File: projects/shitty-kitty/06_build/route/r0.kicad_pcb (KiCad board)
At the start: 4 copper layers, 130 x 75 mm, 82 parts, among them J1 DC-005C-20A 12V, J2 TYPE-C-31-M-12, J3 ELECTRODES INNER, J4 ELECTRODES OUTER, J5 MOTOR NEMA17, J6 ENDSTOP TERM, J8 HOST 1x6, Q1 AOD4185 revpol, SW1 TS-1187A BOOT, SW2 TS-1187A RESET, U1 ESP32-S3-WROOM-1-N8R2, U2 TMC2209-LA-T, U3 MPR121QR2 0x5A, U4 MPR121QR2 0x5B, U5 MPR121QR2 0x5C, U6 MPR121QR2 0x5D, U7 LIS2DH12TR, U8 AP63205WU-7, U9 AMS1117-3.3

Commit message: shitty-kitty: fab-floor pin for KRT (no advanced-via escalation), honest hole floors (h2h 0.3/holeclr 0.2), ELEC/3V3 width floors match router grading, route_surgery tool, stitcher fine-pitch GND rescue + via-pad joins
Co-Authored-By: Claude Fable 5 <noreply@anthropic.com>
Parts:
- moved C12 16.4 mm to (154.0, 104.5)
- moved R9 11.7 mm to (149.5, 108.0)
- moved C26 6.52 mm to (154.0, 101.5)
- moved C13 3.54 mm to (154.0, 107.5)
- moved C16 3.54 mm to (154.0, 110.5)
- turned U7 to 90 degrees

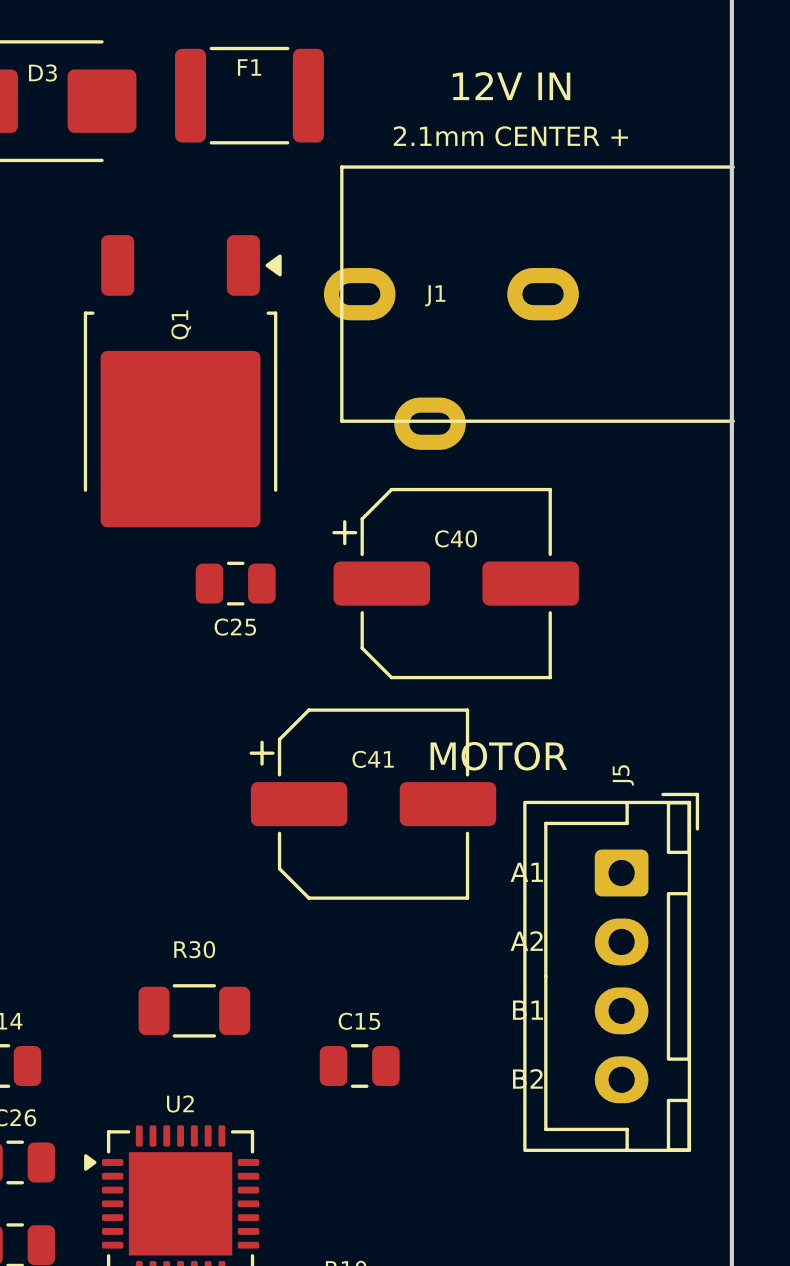
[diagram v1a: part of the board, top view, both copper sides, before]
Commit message: shitty-kitty: WIP CHECKPOINT (not a gate) — routing surgery mid-flight, 18 DRC violations remain (6 clearance/5 hole_clr/6 h2h/1 conn_width from the SDA-via relocation), 0 unconnected. Route-surgery tooling: route_taps/route_unlock/lift_floors. Agent died on Fable credit wall; preserving work
Co-Authored-By: Claude Fable 5 <noreply@anthropic.com>
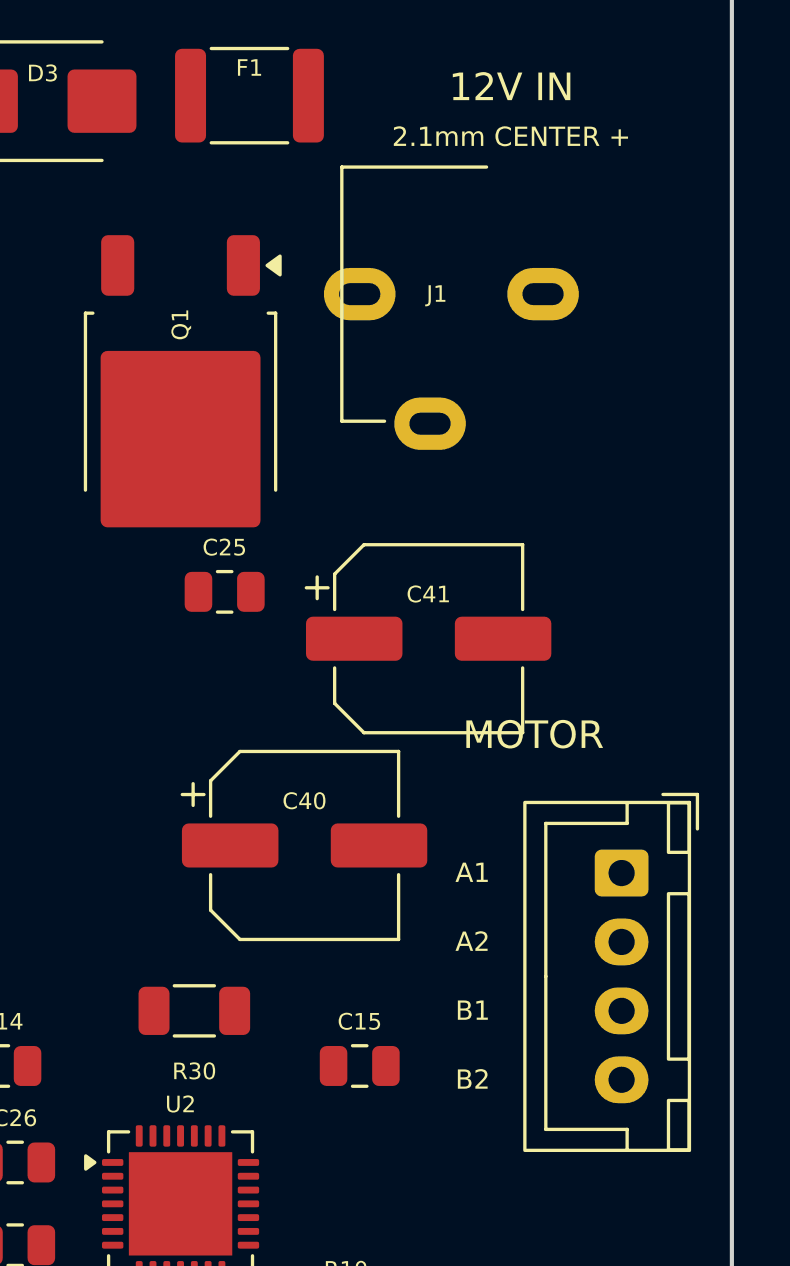
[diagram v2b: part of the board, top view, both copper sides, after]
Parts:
- moved C40 11.0 mm to (164.5, 90.0)
- moved C41 6.32 mm to (169.0, 82.5)
- moved C25 0.50 mm to (161.6, 80.8)
